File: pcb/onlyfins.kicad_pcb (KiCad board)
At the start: 2 copper layers, 34 parts, among them J2 12V_in, Q1 BSS138, U1 L7805

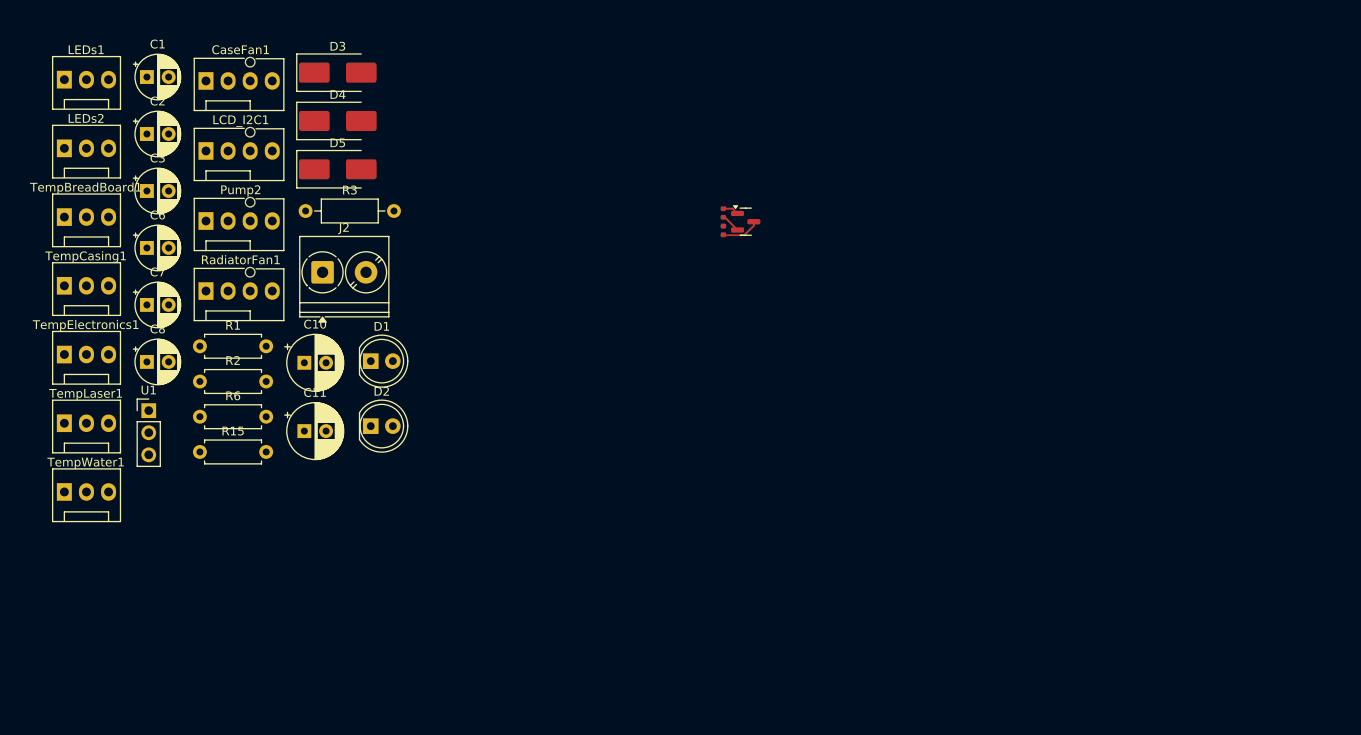
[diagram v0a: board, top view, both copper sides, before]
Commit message: Adding subsheets for fan control
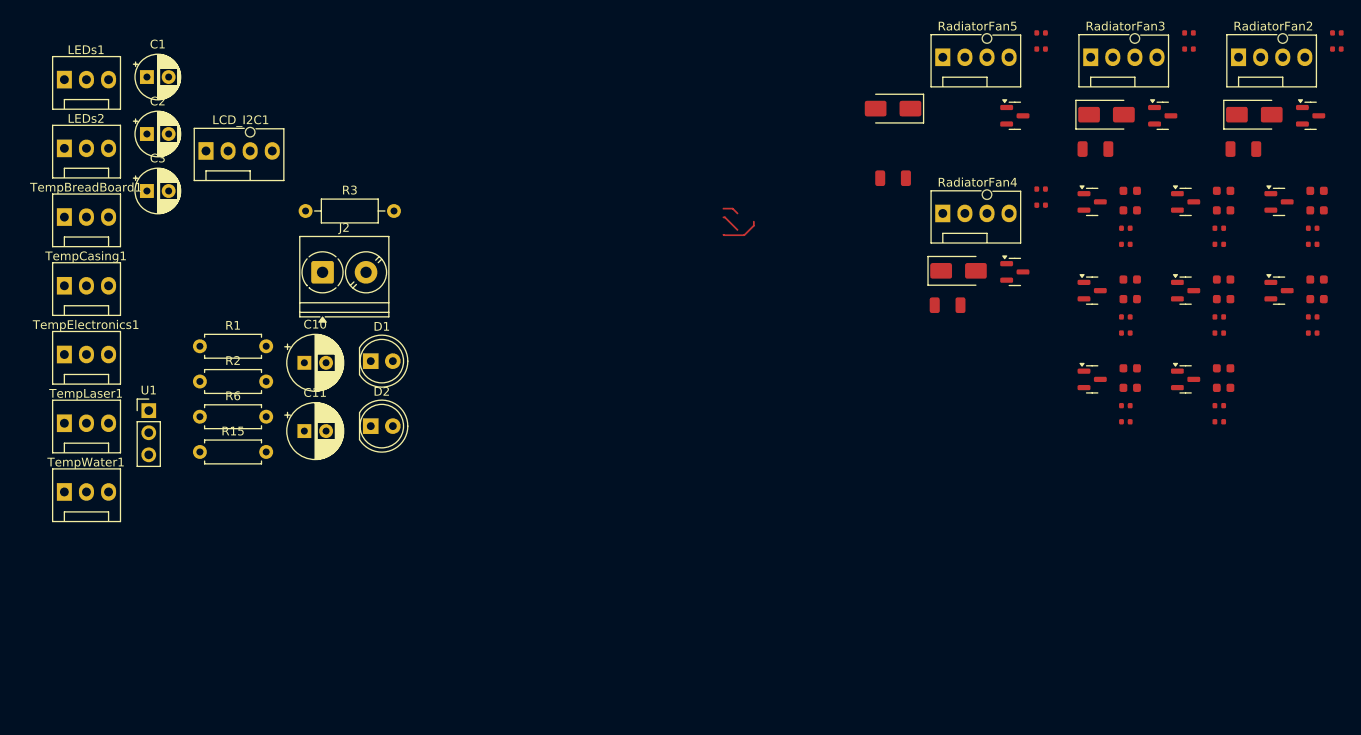
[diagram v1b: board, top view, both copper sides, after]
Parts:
- removed CaseFan1, Pump2, RadiatorFan1: Fan_4pin, Connector:FanPinHeader_1x04_P2.54mm_Vertical
- removed D3, D4, D5: D_Small_ALT, Diode_SMD:D_SMB_Handsoldering
- added C12: 100nF, PCM_JLCPCB:C_0603, F.Cu at (205.3, 104.8)
- added C13: 100nF, PCM_JLCPCB:C_0603, F.Cu at (216.0, 84.5)
- added C14: 100nF, PCM_JLCPCB:C_0603, F.Cu at (205.3, 84.5)
- added C15: 100nF, PCM_JLCPCB:C_0603, F.Cu at (205.3, 94.7)
- added C16: 100nF, PCM_JLCPCB:C_0603, F.Cu at (216.0, 107.1)
- added C17: 100nF, PCM_JLCPCB:C_0603, F.Cu at (226.7, 96.9)
- added C18: 100nF, PCM_JLCPCB:C_0603, F.Cu at (226.7, 86.7)
- added C19: 100nF, PCM_JLCPCB:C_0603, F.Cu at (216.0, 96.9)
- added C20: 100nF, PCM_JLCPCB:C_0603, F.Cu at (205.3, 107.1)
- added C21: 100nF, PCM_JLCPCB:C_0603, F.Cu at (216.0, 86.7)
- added C22: 100nF, PCM_JLCPCB:C_0603, F.Cu at (205.3, 86.7)
- added C23: 100nF, PCM_JLCPCB:C_0603, F.Cu at (205.3, 96.9)
- added C24: 22uF, PCM_JLCPCB:C_1206, F.Cu at (218.3, 79.7)
- added C25: 22uF, PCM_JLCPCB:C_1206, F.Cu at (201.3, 79.7)
- added C26: 22uF, PCM_JLCPCB:C_1206, F.Cu at (184.3, 97.6)
- added C27: 22uF, PCM_JLCPCB:C_1206, F.Cu at (178.0, 83.0)
- added C9: 100nF, PCM_JLCPCB:C_0603, F.Cu at (216.0, 94.7)
- added D6: SS14, PCM_JLCPCB:D_SMA, F.Cu at (219.5, 75.7)
- added D7: SS14, PCM_JLCPCB:D_SMA, F.Cu at (202.5, 75.7)
- added D8: SS14, PCM_JLCPCB:D_SMA, F.Cu at (185.5, 93.7)
- added D9: SS14, PCM_JLCPCB:D_SMA, F.Cu at (178.0, 75.0)
- added Q10: AO3400A, PCM_JLCPCB:Q_SOT-23, F.Cu at (192.0, 75.8)
- added Q11: BSS138, PCM_JLCPCB:Q_SOT-23, F.Cu at (200.9, 85.7)
- added Q12: BSS138, PCM_JLCPCB:Q_SOT-23, F.Cu at (200.9, 95.9)
- added Q2: AO3400A, PCM_JLCPCB:Q_SOT-23, F.Cu at (226.0, 75.8)
- added Q3: BSS138, PCM_JLCPCB:Q_SOT-23, F.Cu at (222.4, 95.9)
- added Q4: AO3400A, PCM_JLCPCB:Q_SOT-23, F.Cu at (209.0, 75.8)
- added Q5: BSS138, PCM_JLCPCB:Q_SOT-23, F.Cu at (222.4, 85.7)
- added Q6: BSS138, PCM_JLCPCB:Q_SOT-23, F.Cu at (211.6, 95.9)
- added Q7: AO3400A, PCM_JLCPCB:Q_SOT-23, F.Cu at (192.0, 93.8)
- added Q8: BSS138, PCM_JLCPCB:Q_SOT-23, F.Cu at (200.9, 106.1)
- added Q9: BSS138, PCM_JLCPCB:Q_SOT-23, F.Cu at (211.6, 85.7)
- added R17: 10kΩ, PCM_JLCPCB:R_0402, F.Cu at (229.0, 66.3)
- added R18: 1kΩ, PCM_JLCPCB:R_0402, F.Cu at (229.0, 68.2)
- added R19: 10kΩ, PCM_JLCPCB:R_0402, F.Cu at (226.2, 99.0)
- added R20: 10kΩ, PCM_JLCPCB:R_0402, F.Cu at (226.2, 100.8)
- added R21: 1kΩ, PCM_JLCPCB:R_0402, F.Cu at (212.0, 66.3)
- added R22: 10kΩ, PCM_JLCPCB:R_0402, F.Cu at (212.0, 68.2)
- added R23: 10kΩ, PCM_JLCPCB:R_0402, F.Cu at (226.2, 88.8)
- added R24: 10kΩ, PCM_JLCPCB:R_0402, F.Cu at (226.2, 90.6)
- added R25: 10kΩ, PCM_JLCPCB:R_0402, F.Cu at (215.5, 99.0)
- added R26: 10kΩ, PCM_JLCPCB:R_0402, F.Cu at (215.5, 100.8)
- added R27: 1kΩ, PCM_JLCPCB:R_0402, F.Cu at (195.0, 84.2)
- added R28: 10kΩ, PCM_JLCPCB:R_0402, F.Cu at (195.0, 86.1)
- added R29: 10kΩ, PCM_JLCPCB:R_0402, F.Cu at (204.8, 109.2)
- added R30: 10kΩ, PCM_JLCPCB:R_0402, F.Cu at (204.8, 111.0)
- added R31: 10kΩ, PCM_JLCPCB:R_0402, F.Cu at (215.5, 88.8)
- added R32: 10kΩ, PCM_JLCPCB:R_0402, F.Cu at (215.5, 90.6)
- added R33: 1kΩ, PCM_JLCPCB:R_0402, F.Cu at (195.0, 66.3)
- added R34: 10kΩ, PCM_JLCPCB:R_0402, F.Cu at (195.0, 68.2)
- added R35: 10kΩ, PCM_JLCPCB:R_0402, F.Cu at (204.8, 88.8)
- added R36: 10kΩ, PCM_JLCPCB:R_0402, F.Cu at (204.8, 90.6)
- added R37: 10kΩ, PCM_JLCPCB:R_0402, F.Cu at (204.8, 99.0)
- added R38: 10kΩ, PCM_JLCPCB:R_0402, F.Cu at (204.8, 100.8)
- added RadiatorFan2: Fan_4pin, Connector:FanPinHeader_1x04_P2.54mm_Vertical, F.Cu at (217.7, 69.1)
- added RadiatorFan3: Fan_4pin, Connector:FanPinHeader_1x04_P2.54mm_Vertical, F.Cu at (200.7, 69.1)
- added RadiatorFan4: Fan_4pin, Connector:FanPinHeader_1x04_P2.54mm_Vertical, F.Cu at (183.7, 87.0)
- added RadiatorFan5: Fan_4pin, Connector:FanPinHeader_1x04_P2.54mm_Vertical, F.Cu at (183.7, 69.1)
- C6, C7, C8: value 10u -> 100nF; footprint Capacitor_THT:CP_Radial_D5.0mm_P2.50mm -> PCM_JLCPCB:C_0603
- moved C8 135.9 mm to (226.7, 84.5)
- moved C7 134.5 mm to (226.7, 94.7)
- moved C6 124.5 mm to (216.0, 104.8)
- moved R4 61.2 mm to (215.5, 109.2), turned to 0 degrees
- moved R5 61.1 mm to (215.5, 111.0), turned to 0 degrees
- moved Q1 53.7 mm to (211.6, 106.1)
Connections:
- net /LV renamed /Fan 1/level_shifter/sig_lv
- C6 pad 1: +12V -> /Fan 1/level_shifter/vcc_hv
- C6 pad 2: GND -> /Fan 1/level_shifter/sig_hv
- C7 pad 1: +12V -> /Fan 1/level_shifter1/vcc_hv
- C7 pad 2: GND -> /Fan 1/level_shifter1/sig_hv
- C8 pad 1: +12V -> /Fan 2/level_shifter/vcc_hv
- C8 pad 2: GND -> /Fan 2/level_shifter/sig_hv
- Q1 pad 1: +3V3 -> /Fan 1/level_shifter/vcc_lv
- Q1 pad 3: /HV -> /Fan 1/level_shifter/sig_hv
- R4 pad 1: +3V3 -> /Fan 1/level_shifter/vcc_lv
- R5 pad 1: +5V -> /Fan 1/level_shifter/vcc_hv
- R5 pad 2: /HV -> /Fan 1/level_shifter/sig_hv
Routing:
- net (no net): track 0.00 -> 6.65 mm
- net /HV: track 4.43 -> 0.00 mm
- net /Fan 1/level_shifter/sig_lv: track 2.22 -> 0.00 mm

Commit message: Add temperature sensors
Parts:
- removed R3: 4.7k, Resistor_THT:R_Axial_DIN0207_L6.3mm_D2.5mm_P10.16mm_Horizontal
- removed TempBreadBoard1, TempCasing1, TempElectronics1, TempLaser1, TempWater1: DigiTempSens1, Connector:FanPinHeader_1x03_P2.54mm_Vertical
- added C28: 100nF, PCM_JLCPCB:C_0603, F.Cu at (150.3, 144.5)
- added C29: 100nF, PCM_JLCPCB:C_0603, F.Cu at (165.5, 144.5)
- added C30: 100nF, PCM_JLCPCB:C_0603, F.Cu at (150.3, 130.9)
- added C31: 100nF, PCM_JLCPCB:C_0603, F.Cu at (165.5, 130.9)
- added J1: Temp1, TerminalBlock_4Ucon:TerminalBlock_4Ucon_1x03_P3.50mm_Horizontal, F.Cu at (151.5, 138.5)
- added J3: Temp1, TerminalBlock_4Ucon:TerminalBlock_4Ucon_1x03_P3.50mm_Horizontal, F.Cu at (166.7, 138.5)
- added J4: Temp1, TerminalBlock_4Ucon:TerminalBlock_4Ucon_1x03_P3.50mm_Horizontal, F.Cu at (151.5, 124.9)
- added J5: Temp1, TerminalBlock_4Ucon:TerminalBlock_4Ucon_1x03_P3.50mm_Horizontal, F.Cu at (166.7, 124.9)
- added R10: 4.7kΩ, PCM_JLCPCB:R_0402, F.Cu at (168.9, 130.7)
- added R7: 4.7kΩ, PCM_JLCPCB:R_0402, F.Cu at (153.6, 144.3)
- added R8: 4.7kΩ, PCM_JLCPCB:R_0402, F.Cu at (168.9, 144.3)
- added R9: 4.7kΩ, PCM_JLCPCB:R_0402, F.Cu at (153.6, 130.7)
